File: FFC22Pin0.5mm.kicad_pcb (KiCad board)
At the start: 2 copper layers, 111.5 x 104.6 mm, 48 parts

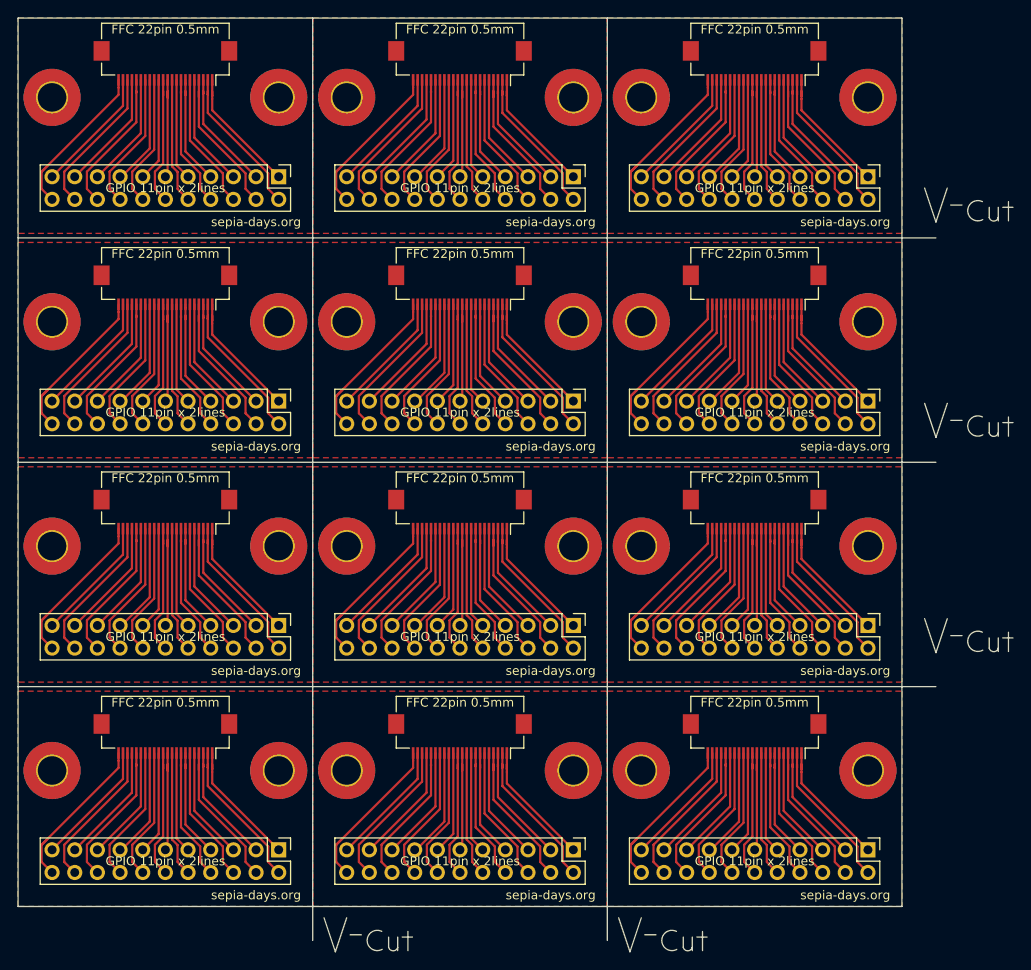
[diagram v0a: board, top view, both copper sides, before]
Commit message: 基板裏にベタ追加、ビア追加、パッドをベタに接続、配線をより対称に近づけた
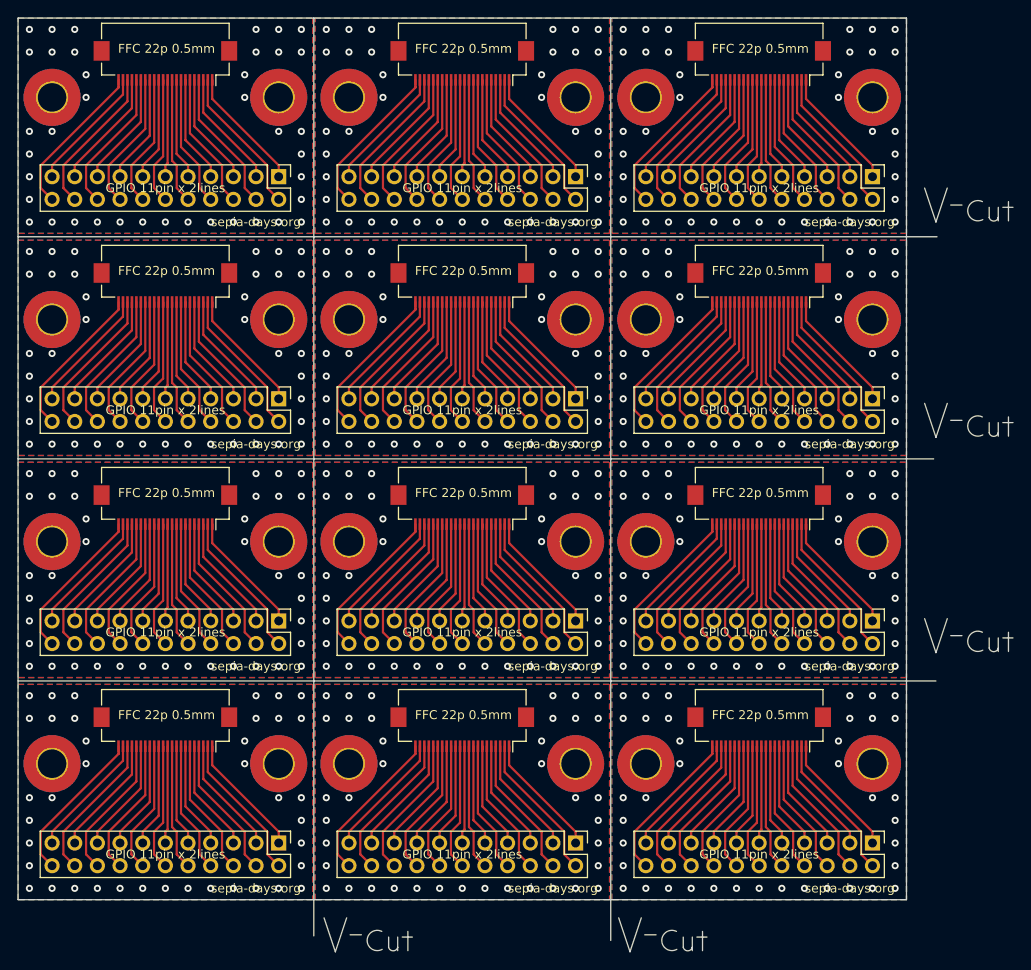
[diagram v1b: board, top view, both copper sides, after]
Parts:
- removed FFC 22pin 0.5mm: GPIO22Pin, Connector_FFC-FPC:Hirose_FH12-22S-0.5SH_1x22-1MP_P0.50mm_Horizontal (x12)
- removed the GPIO 11pin x 2lines at (148.6, 115.1)
- removed the GPIO 11pin x 2lines at (82.5, 115.1)
- removed the GPIO 11pin x 2lines at (82.5, 89.9)
- removed the GPIO 11pin x 2lines at (148.6, 89.9)
- removed the GPIO 11pin x 2lines at (148.6, 140.2)
- removed the GPIO 11pin x 2lines at (148.6, 64.8)
- removed the GPIO 11pin x 2lines at (115.6, 115.1)
- removed the GPIO 11pin x 2lines at (115.6, 89.9)
- removed the GPIO 11pin x 2lines at (115.6, 140.2)
- removed the GPIO 11pin x 2lines at (115.6, 64.8)
- removed the GPIO 11pin x 2lines at (82.5, 140.2)
- removed the H1 at (123.2, 131.3)
- removed the H1 at (57.1, 106.2)
- removed the H1 at (57.1, 81.0)
- removed the H1 at (123.2, 81.0)
- removed the H1 at (123.2, 106.2)
- removed the H1 at (123.2, 55.9)
- removed the H1 at (90.2, 131.3)
- removed the H1 at (90.2, 81.0)
- removed the H1 at (90.2, 106.2)
- removed the H1 at (90.2, 55.9)
- removed the H1 at (57.1, 131.3)
- removed the H2 at (148.6, 131.3)
- removed the H2 at (82.5, 106.2)
- removed the H2 at (82.5, 81.0)
- removed the H2 at (148.6, 81.0)
- removed the H2 at (148.6, 106.2)
- removed the H2 at (148.6, 55.9)
- removed the H2 at (115.6, 131.3)
- removed the H2 at (115.6, 81.0)
- removed the H2 at (115.6, 106.2)
- removed the H2 at (115.6, 55.9)
- removed the H2 at (82.5, 131.3)
- added FFC 22p 0.5mm: GPIO22Pin, Connector_FFC-FPC:Hirose_FH12-22S-0.5SH_1x22-1MP_P0.50mm_Horizontal, F.Cu at (103.1, 101.9)
- added FFC 22p 0.5mm: GPIO22Pin, Connector_FFC-FPC:Hirose_FH12-22S-0.5SH_1x22-1MP_P0.50mm_Horizontal, F.Cu at (136.4, 52.1)
- added FFC 22p 0.5mm: GPIO22Pin, Connector_FFC-FPC:Hirose_FH12-22S-0.5SH_1x22-1MP_P0.50mm_Horizontal, F.Cu at (103.1, 52.1)
- added FFC 22p 0.5mm: GPIO22Pin, Connector_FFC-FPC:Hirose_FH12-22S-0.5SH_1x22-1MP_P0.50mm_Horizontal, F.Cu at (69.8, 52.1)
- added FFC 22p 0.5mm: GPIO22Pin, Connector_FFC-FPC:Hirose_FH12-22S-0.5SH_1x22-1MP_P0.50mm_Horizontal, F.Cu at (103.1, 126.7)
- added FFC 22p 0.5mm: GPIO22Pin, Connector_FFC-FPC:Hirose_FH12-22S-0.5SH_1x22-1MP_P0.50mm_Horizontal, F.Cu at (69.8, 126.7)
- added FFC 22p 0.5mm: GPIO22Pin, Connector_FFC-FPC:Hirose_FH12-22S-0.5SH_1x22-1MP_P0.50mm_Horizontal, F.Cu at (136.4, 101.9)
- added FFC 22p 0.5mm: GPIO22Pin, Connector_FFC-FPC:Hirose_FH12-22S-0.5SH_1x22-1MP_P0.50mm_Horizontal, F.Cu at (136.4, 126.7)
- added FFC 22p 0.5mm: GPIO22Pin, Connector_FFC-FPC:Hirose_FH12-22S-0.5SH_1x22-1MP_P0.50mm_Horizontal, F.Cu at (69.8, 101.9)
- added FFC 22p 0.5mm: GPIO22Pin, Connector_FFC-FPC:Hirose_FH12-22S-0.5SH_1x22-1MP_P0.50mm_Horizontal, F.Cu at (103.1, 77.0)
- added FFC 22p 0.5mm: GPIO22Pin, Connector_FFC-FPC:Hirose_FH12-22S-0.5SH_1x22-1MP_P0.50mm_Horizontal, F.Cu at (136.4, 77.0)
- added FFC 22p 0.5mm: GPIO22Pin, Connector_FFC-FPC:Hirose_FH12-22S-0.5SH_1x22-1MP_P0.50mm_Horizontal, F.Cu at (69.8, 77.0)
- added GPIO 11pin x 2lines: GPIO22Pin, Connector_PinHeader_2.54mm:PinHeader_2x11_P2.54mm_Vertical, F.Cu at (115.8, 139.4)
- added GPIO 11pin x 2lines: GPIO22Pin, Connector_PinHeader_2.54mm:PinHeader_2x11_P2.54mm_Vertical, F.Cu at (149.1, 64.8)
- added GPIO 11pin x 2lines: GPIO22Pin, Connector_PinHeader_2.54mm:PinHeader_2x11_P2.54mm_Vertical, F.Cu at (115.8, 64.8)
- added GPIO 11pin x 2lines: GPIO22Pin, Connector_PinHeader_2.54mm:PinHeader_2x11_P2.54mm_Vertical, F.Cu at (149.1, 114.6)
- added GPIO 11pin x 2lines: GPIO22Pin, Connector_PinHeader_2.54mm:PinHeader_2x11_P2.54mm_Vertical, F.Cu at (115.8, 114.6)
- added GPIO 11pin x 2lines: GPIO22Pin, Connector_PinHeader_2.54mm:PinHeader_2x11_P2.54mm_Vertical, F.Cu at (82.5, 139.4)
- added GPIO 11pin x 2lines: GPIO22Pin, Connector_PinHeader_2.54mm:PinHeader_2x11_P2.54mm_Vertical, F.Cu at (149.1, 139.4)
- added GPIO 11pin x 2lines: GPIO22Pin, Connector_PinHeader_2.54mm:PinHeader_2x11_P2.54mm_Vertical, F.Cu at (82.5, 114.6)
- added GPIO 11pin x 2lines: GPIO22Pin, Connector_PinHeader_2.54mm:PinHeader_2x11_P2.54mm_Vertical, F.Cu at (149.1, 89.7)
- added GPIO 11pin x 2lines: GPIO22Pin, Connector_PinHeader_2.54mm:PinHeader_2x11_P2.54mm_Vertical, F.Cu at (115.8, 89.7)
- added GPIO 11pin x 2lines: GPIO22Pin, Connector_PinHeader_2.54mm:PinHeader_2x11_P2.54mm_Vertical, F.Cu at (82.5, 89.7)
- added H1: MountingHole_Pad, MountingHole:MountingHole_3.2mm_M3_Pad_TopBottom, F.Cu at (123.7, 130.6)
- added H1: MountingHole_Pad, MountingHole:MountingHole_3.2mm_M3_Pad_TopBottom, F.Cu at (123.7, 55.9)
- added H1: MountingHole_Pad, MountingHole:MountingHole_3.2mm_M3_Pad_TopBottom, F.Cu at (90.4, 55.9)
- added H1: MountingHole_Pad, MountingHole:MountingHole_3.2mm_M3_Pad_TopBottom, F.Cu at (57.1, 130.6)
- added H1: MountingHole_Pad, MountingHole:MountingHole_3.2mm_M3_Pad_TopBottom, F.Cu at (90.4, 105.7)
- added H1: MountingHole_Pad, MountingHole:MountingHole_3.2mm_M3_Pad_TopBottom, F.Cu at (90.4, 130.6)
- added H1: MountingHole_Pad, MountingHole:MountingHole_3.2mm_M3_Pad_TopBottom, F.Cu at (123.7, 105.7)
- added H1: MountingHole_Pad, MountingHole:MountingHole_3.2mm_M3_Pad_TopBottom, F.Cu at (57.1, 105.7)
- added H1: MountingHole_Pad, MountingHole:MountingHole_3.2mm_M3_Pad_TopBottom, F.Cu at (90.4, 80.8)
- added H1: MountingHole_Pad, MountingHole:MountingHole_3.2mm_M3_Pad_TopBottom, F.Cu at (123.7, 80.8)
- added H1: MountingHole_Pad, MountingHole:MountingHole_3.2mm_M3_Pad_TopBottom, F.Cu at (57.1, 80.8)
- added H2: MountingHole_Pad, MountingHole:MountingHole_3.2mm_M3_Pad_TopBottom, F.Cu at (115.8, 130.6)
- added H2: MountingHole_Pad, MountingHole:MountingHole_3.2mm_M3_Pad_TopBottom, F.Cu at (149.1, 55.9)
- added H2: MountingHole_Pad, MountingHole:MountingHole_3.2mm_M3_Pad_TopBottom, F.Cu at (115.8, 55.9)
- added H2: MountingHole_Pad, MountingHole:MountingHole_3.2mm_M3_Pad_TopBottom, F.Cu at (149.1, 130.6)
- added H2: MountingHole_Pad, MountingHole:MountingHole_3.2mm_M3_Pad_TopBottom, F.Cu at (115.8, 105.7)
- added H2: MountingHole_Pad, MountingHole:MountingHole_3.2mm_M3_Pad_TopBottom, F.Cu at (82.5, 130.6)
- added H2: MountingHole_Pad, MountingHole:MountingHole_3.2mm_M3_Pad_TopBottom, F.Cu at (149.1, 105.7)
- added H2: MountingHole_Pad, MountingHole:MountingHole_3.2mm_M3_Pad_TopBottom, F.Cu at (82.5, 105.7)
- added H2: MountingHole_Pad, MountingHole:MountingHole_3.2mm_M3_Pad_TopBottom, F.Cu at (115.8, 80.8)
- added H2: MountingHole_Pad, MountingHole:MountingHole_3.2mm_M3_Pad_TopBottom, F.Cu at (149.1, 80.8)
- added H2: MountingHole_Pad, MountingHole:MountingHole_3.2mm_M3_Pad_TopBottom, F.Cu at (82.5, 80.8)
- H1, H2: value MountingHole -> MountingHole_Pad
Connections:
- H1 pad 1: (no net) -> GND
- H2 pad 1: (no net) -> GND
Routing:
- net (no net): track 3470.6 -> 3444.4 mm, vias 0 -> 429
- net Net-(GPIO1-Pad22): track 18.4 -> 17.5 mm
- net Net-(GPIO1-Pad4): track 16.7 -> 16.0 mm
- net GND: vias 0 -> 39
- added copper zone on B.Cu, net (none)
- added copper zone on B.Cu, net GND
- added copper zone on F.Cu, net GND
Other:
- outline, holes or cut-outs redrawn

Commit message: DRCによるカット分周辺のベタ削除
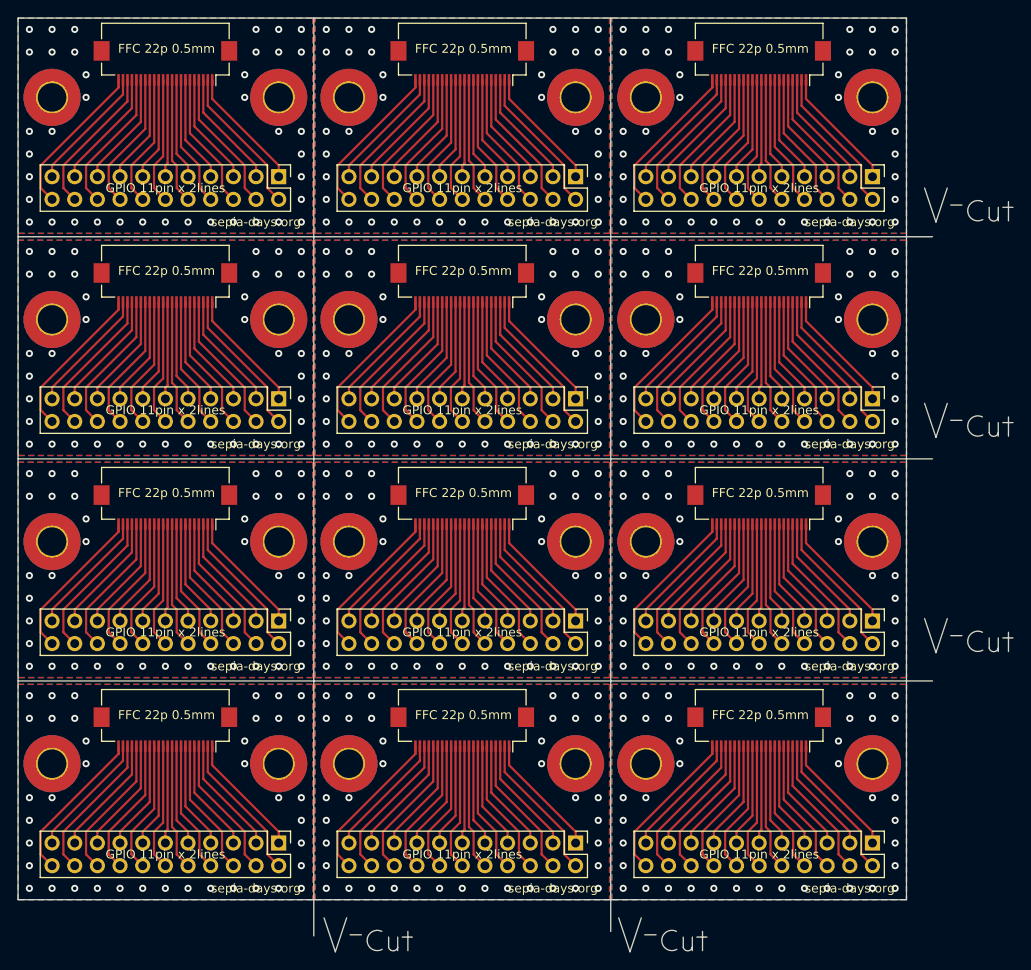
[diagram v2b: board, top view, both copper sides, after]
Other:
- outline, holes or cut-outs redrawn
